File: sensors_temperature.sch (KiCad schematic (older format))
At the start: 3 parts

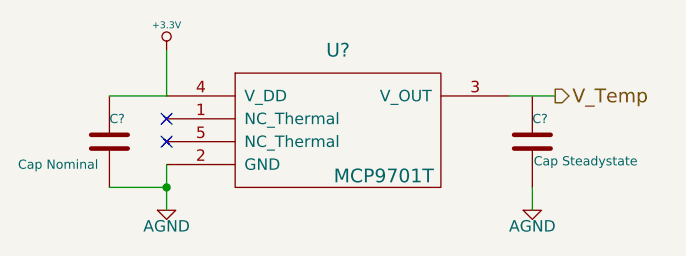
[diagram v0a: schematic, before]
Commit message: Various components added
USB conn, general outputs, brake signal, touch sensor
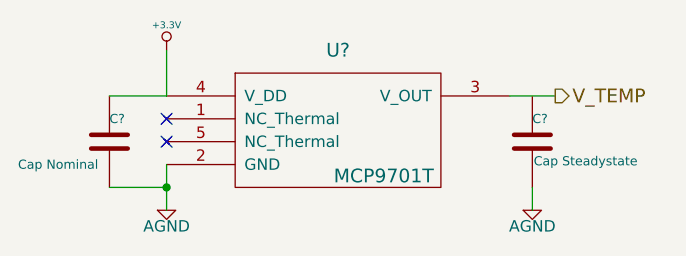
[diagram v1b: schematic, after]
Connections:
- net V_Temp renamed V_TEMP
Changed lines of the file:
@@
 $Descr A4 11693 8268
 encoding utf-8
-Sheet 11 14
+Sheet 6 11
 Title ""
-Date "10 nov 2013"
+Date "11 nov 2013"
 Rev ""
 Comp ""
@@
 	1300 850  1300 1050
 Text HLabel 3000 1050 2    60   Output ~ 0
-V_Temp
+V_TEMP
 Wire Wire Line
 	2900 1550 2900 1450
